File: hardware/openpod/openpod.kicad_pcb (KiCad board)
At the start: 2 copper layers, 42.8 x 59.9 mm, 14 parts, among them J1 SJ-43515TS-SMT-TR

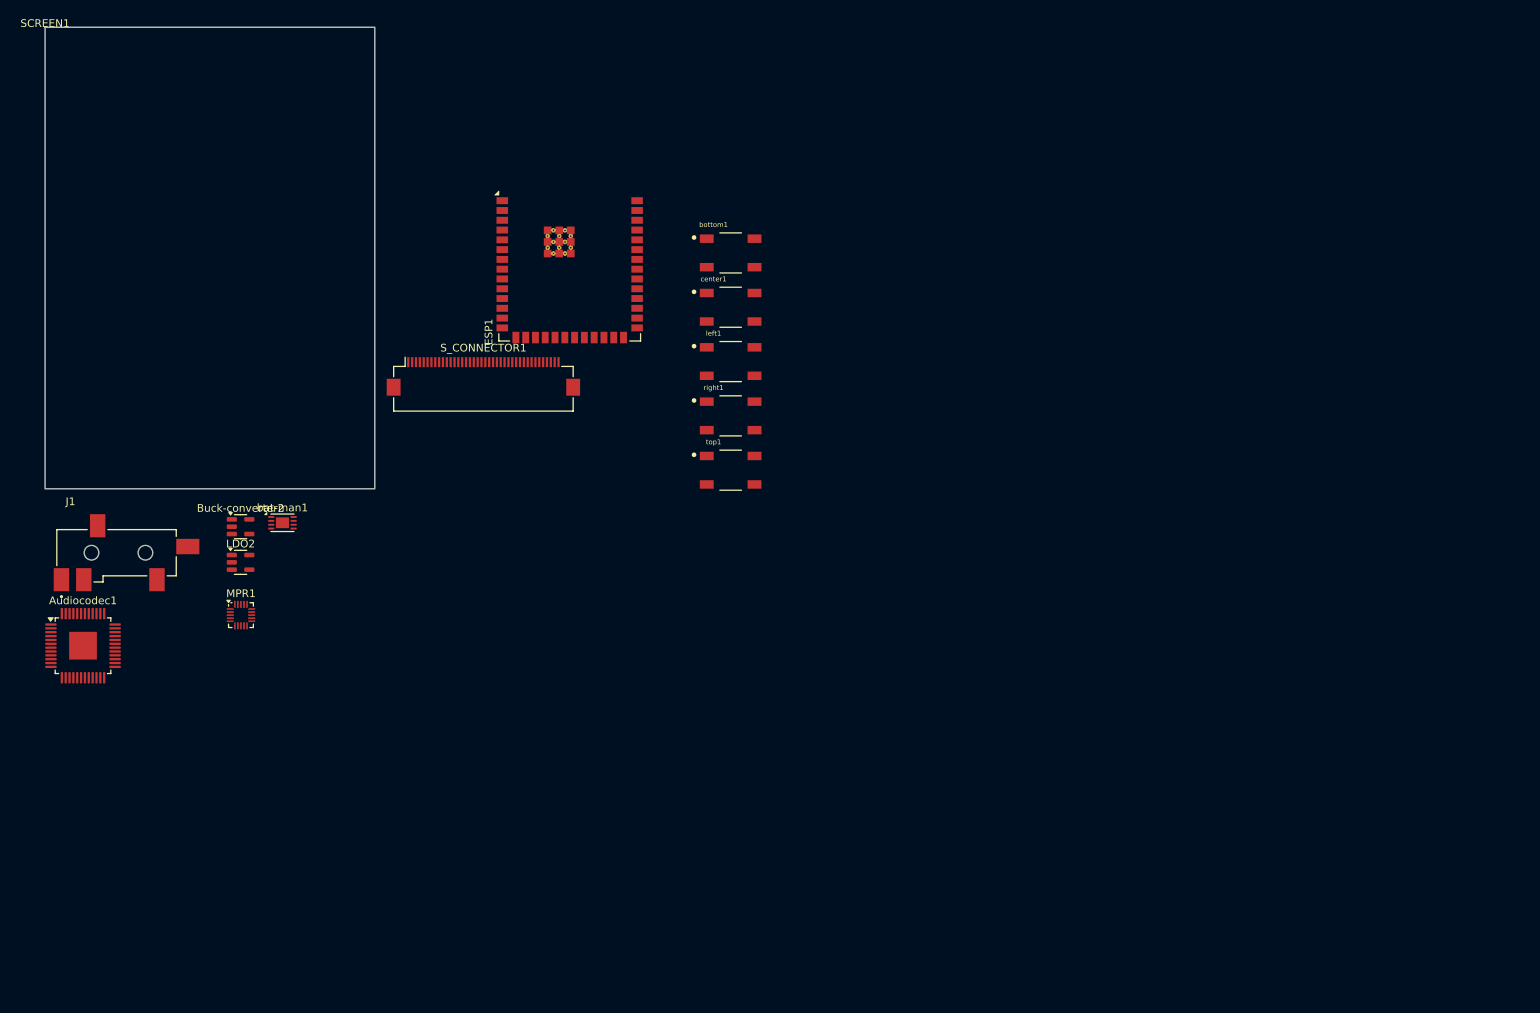
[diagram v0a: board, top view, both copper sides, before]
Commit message: designed clickwheel and see if mpr121 can fit on it
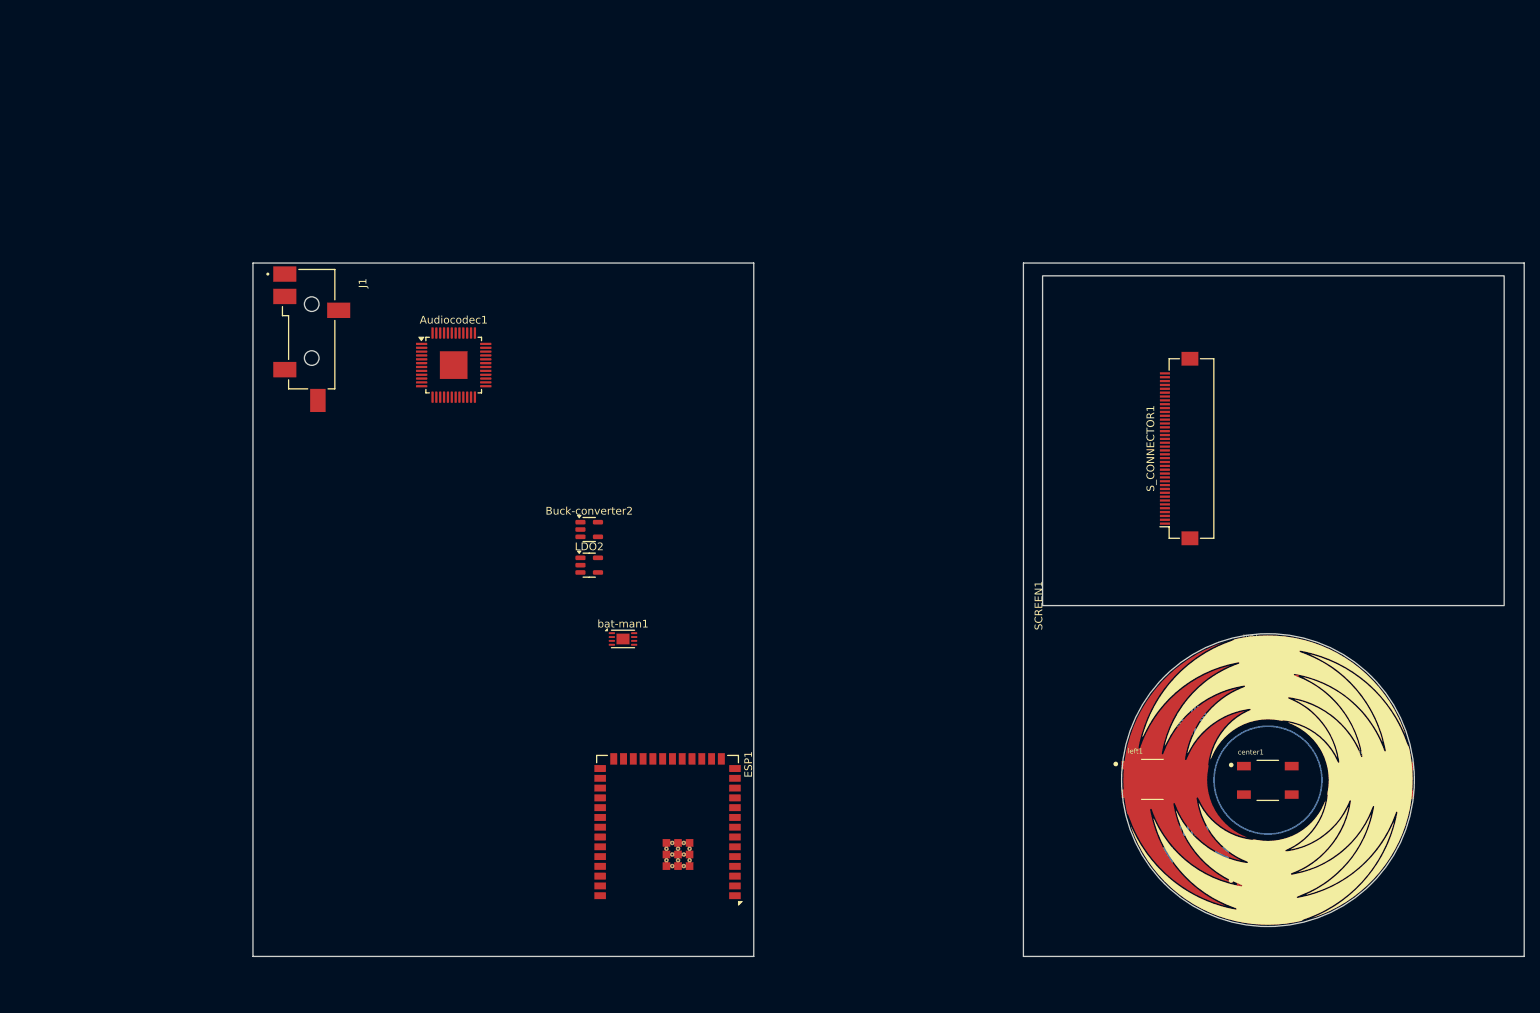
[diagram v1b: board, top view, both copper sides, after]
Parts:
- added Clickwheel1: ~, openpod:clickwheel_1, F.Cu at (231.7, 117.1)
- added clickwheel-connector1: ~, Connector_FFC-FPC:Hirose_FH12-8S-0.5SH_1x08-1MP_P0.50mm_Horizontal, B.Cu at (222.1, 125.5)
- ESP1: footprint openpod:ESP32-S3-WROOM-2 -> RF_Module:ESP32-S3-WROOM-2
- MPR1: footprint Package_DFN_QFN:UQFN-20_3x3mm_P0.4mm -> openpod:mpr121qr2; moved to B.Cu
- moved SCREEN1 149.7 mm to (202.5, 94.5), turned to 90 degrees
- moved MPR1 124.2 mm to (221.9, 109.3), turned to 90 degrees
- moved bottom1 108.7 mm to (231.7, 132.1)
- moved right1 97.0 mm to (246.7, 117.1)
- moved center1 92.9 mm to (231.7, 117.1)
- moved S_CONNECTOR1 90.8 mm to (220.2, 74.1), turned to 90 degrees
- moved ESP1 80.7 mm to (153.8, 126.9), turned to 180 degrees
- moved left1 77.1 mm to (216.7, 117.0)
- moved top1 74.2 mm to (231.7, 102.2)
- moved Audiocodec1 60.3 mm to (126.1, 63.2)
- moved J1 49.1 mm to (104.1, 51.4), turned to -90 degrees
- moved bat-man1 46.7 mm to (148.0, 98.8)
- moved Buck-converter2 45.3 mm to (143.6, 84.6)
- moved LDO2 45.3 mm to (143.6, 89.2)
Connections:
- MPR1 pad 1: unconnected-(MPR1-~{IRQ}-Pad1) -> Net-(MPR1-~{IRQ})
- MPR1 pad 15: unconnected-(MPR1-LED3/ELE7-Pad15) -> Net-(Clickwheel1-right)
- MPR1 pad 16: unconnected-(MPR1-LED4/ELE8-Pad16) -> Net-(Clickwheel1-top)
- MPR1 pad 19: unconnected-(MPR1-LED7/ELE11-Pad19) -> Net-(Clickwheel1-bottom)
- MPR1 pad 2: unconnected-(MPR1-SCL-Pad2) -> Net-(MPR1-SCL)
- MPR1 pad 20: unconnected-(MPR1-VDD-Pad20) -> Net-(MPR1-VDD)
- MPR1 pad 3: unconnected-(MPR1-SDA-Pad3) -> Net-(MPR1-SDA)
- MPR1 pad 4: unconnected-(MPR1-ADDR-Pad4) -> Net-(MPR1-ADDR)
- MPR1 pad 5: unconnected-(MPR1-VREG-Pad5) -> Net-(MPR1-VREG)
- MPR1 pad 6: unconnected-(MPR1-VSS-Pad6) -> Net-(MPR1-VSS)
- MPR1 pad 7: unconnected-(MPR1-REXT-Pad7) -> Net-(MPR1-REXT)
- MPR1 pad 9: unconnected-(MPR1-ELE1-Pad9) -> Net-(Clickwheel1-left)
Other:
- board size 42.8 x 59.9 mm -> 165 x 90 mm

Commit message: update power and audio
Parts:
- moved S_CONNECTOR1 63.4 mm to (157.3, 66.4)
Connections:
- clickwheel-connector1 pad 1: Net-(MPR1-REXT) -> Net-(MPR1-VDD)
- clickwheel-connector1 pad 2: Net-(MPR1-VSS) -> Net-(MPR1-~{IRQ})
- clickwheel-connector1 pad 3: Net-(MPR1-VREG) -> Net-(MPR1-SCL)
- clickwheel-connector1 pad 4: Net-(MPR1-ADDR) -> Net-(MPR1-SDA)
- clickwheel-connector1 pad 5: Net-(MPR1-SDA) -> Net-(MPR1-ADDR)
- clickwheel-connector1 pad 6: Net-(MPR1-SCL) -> Net-(MPR1-VREG)
- clickwheel-connector1 pad 7: Net-(MPR1-~{IRQ}) -> Net-(MPR1-VSS)
- clickwheel-connector1 pad 8: Net-(MPR1-VDD) -> Net-(MPR1-REXT)
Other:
- board size 165 x 90 mm -> 65 x 90 mm
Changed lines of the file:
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@@
     (property "Supplier Part number" "CP-43515TSSJTR-ND")
     (attr smd)
-    (fp_text reference "J1" (at 1.175 -10.135 90) (layer "F.SilkS")
+    (fp_text reference "J1" (at 1.175 -10.135 -90) (layer "F.SilkS")
         (effects (font (size 1 1) (thickness 0.15)))
     )
-    (fp_text value "SJ-43515TS-SMT-TR" (at 11.335 3.135 90) (layer "F.Fab")
+    (fp_text value "SJ-43515TS-SMT-TR" (at 11.335 3.135 -90) (layer "F.Fab")
         (effects (font (size 1 1) (thickness 0.15)))
     )
@@
   )
   (footprint "openpod:Hirose_FH12-40S-0.5SH_1x40-1MP_P0.50mm_Horizontal" (layer "F.Cu")
-    (at 220.215 74.075 90)
+    (at 157.298 66.378 90)
     (descr "Hirose FH12, FFC/FPC connector, FH12-40S-0.5SH, 40 Pins per row (https://www.hirose.com/product/en/products/FH12/FH12-24S-0.5SH(55)/), generated with kicad-footprint-generator")
     (tags "connector Hirose FH12 horizontal")
@@
     (descr "Hirose FH12, FFC/FPC connector, FH12-8S-0.5SH, 8 Pins per row (https://www.hirose.com/product/en/products/FH12/FH12-24S-0.5SH(55)/), generated with kicad-footprint-generator")
     (tags "connector Hirose FH12 horizontal")
-    (property "Manufacturer" "")
-    (property "Part number" "")
+    (property "Manufacturer" "Hirose")
+    (property "Part number" "FH12-8S-0.5SH(55)")
     (property "Sheetfile" "buttons.kicad_sch")
     (property "Sheetname" "Buttons")
-    (property "Supplier" "")
-    (property "Supplier Part number" "")
+    (property "Supplier" "DigiKey")
+    (property "Supplier Part number" "H124618TR-ND")
     (attr smd)
     (fp_text reference "clickwheel-connector1" (at 0 3.7) (layer "B.SilkS")
@@
       (stroke (width 0.1) (type solid)) (layer "B.Fab"))
     (pad "1" smd rect (at -1.75 1.85 180) (size 0.3 1.3) (layers "B.Cu" "B.Paste" "B.Mask")
+      (net 150 "Net-(MPR1-VDD)") (pinfunction "VDD") (pintype "power_in"))
+    (pad "2" smd rect (at -1.25 1.85 180) (size 0.3 1.3) (layers "B.Cu" "B.Paste" "B.Mask")
+      (net 139 "Net-(MPR1-~{IRQ})") (pinfunction "IRQ") (pintype "input"))
+    (pad "3" smd rect (at -0.75 1.85 180) (size 0.3 1.3) (layers "B.Cu" "B.Paste" "B.Mask")
+      (net 140 "Net-(MPR1-SCL)") (pinfunction "SCL") (pintype "input"))
+    (pad "4" smd rect (at -0.25 1.85 180) (size 0.3 1.3) (layers "B.Cu" "B.Paste" "B.Mask")
+      (net 141 "Net-(MPR1-SDA)") (pinfunction "SDA") (pintype "bidirectional"))
+    (pad "5" smd rect (at 0.25 1.85 180) (size 0.3 1.3) (layers "B.Cu" "B.Paste" "B.Mask")
+      (net 142 "Net-(MPR1-ADDR)") (pinfunction "ADDR") (pintype "input"))
+    (pad "6" smd rect (at 0.75 1.85 180) (size 0.3 1.3) (layers "B.Cu" "B.Paste" "B.Mask")
+      (net 143 "Net-(MPR1-VREG)") (pinfunction "VREG") (pintype "input"))
+    (pad "7" smd rect (at 1.25 1.85 180) (size 0.3 1.3) (layers "B.Cu" "B.Paste" "B.Mask")
+      (net 144 "Net-(MPR1-VSS)") (pinfunction "VSS") (pintype "power_in"))
+    (pad "8" smd rect (at 1.75 1.85 180) (size 0.3 1.3) (layers "B.Cu" "B.Paste" "B.Mask")
       (net 145 "Net-(MPR1-REXT)") (pinfunction "REXT") (pintype "passive"))
-    (pad "2" smd rect (at -1.25 1.85 180) (size 0.3 1.3) (layers "B.Cu" "B.Paste" "B.Mask")
-      (net 144 "Net-(MPR1-VSS)") (pinfunction "VSS") (pintype "power_in"))
-    (pad "3" smd rect (at -0.75 1.85 180) (size 0.3 1.3) (layers "B.Cu" "B.Paste" "B.Mask")
-      (net 143 "Net-(MPR1-VREG)") (pinfunction "VREG") (pintype "input"))
-    (pad "4" smd rect (at -0.25 1.85 180) (size 0.3 1.3) (layers "B.Cu" "B.Paste" "B.Mask")
-      (net 142 "Net-(MPR1-ADDR)") (pinfunction "ADDR") (pintype "input"))
-    (pad "5" smd rect (at 0.25 1.85 180) (size 0.3 1.3) (layers "B.Cu" "B.Paste" "B.Mask")
-      (net 141 "Net-(MPR1-SDA)") (pinfunction "SDA") (pintype "bidirectional"))
-    (pad "6" smd rect (at 0.75 1.85 180) (size 0.3 1.3) (layers "B.Cu" "B.Paste" "B.Mask")
-      (net 140 "Net-(MPR1-SCL)") (pinfunction "SCL") (pintype "input"))
-    (pad "7" smd rect (at 1.25 1.85 180) (size 0.3 1.3) (layers "B.Cu" "B.Paste" "B.Mask")
-      (net 139 "Net-(MPR1-~{IRQ})") (pinfunction "IRQ") (pintype "input"))
-    (pad "8" smd rect (at 1.75 1.85 180) (size 0.3 1.3) (layers "B.Cu" "B.Paste" "B.Mask")
-      (net 150 "Net-(MPR1-VDD)") (pinfunction "VDD") (pintype "power_in"))
     (pad "MP" smd rect (at -3.65 -1.4 180) (size 1.8 2.2) (layers "B.Cu" "B.Paste" "B.Mask"))
     (pad "MP" smd rect (at 3.65 -1.4 180) (size 1.8 2.2) (layers "B.Cu" "B.Paste" "B.Mask"))
@@
   (gr_rect (start 200 50) (end 265 140)
     (stroke (width 0.1) (type default)) (fill none) (layer "Edge.Cuts"))
+  (gr_rect (start 102.438 51.689) (end 162.382 94.488)
+    (stroke (width 0.1) (type default)) (fill none) (layer "User.1"))
+  (gr_circle (center 131.7 117) (end 150.7 117)
+    (stroke (width 0.1) (type default)) (fill none) (layer "User.1"))
   (gr_rect (start 100 50) (end 165 140)
-    (stroke (width 0.1) (type default)) (fill none) (layer "Edge.Cuts"))
+    (stroke (width 0.1) (type default)) (fill none) (layer "User.1"))
+  (group "" (id 2323effc-a0d1-4313-aa63-f355f6ec8b0d)
+    (members
+      2688467a-e8e8-472a-93a4-b563cc7689f2
+      444ad04b-41b9-4e0e-83e2-88ab4b3fa3dd
+      a93e316e-5e73-4e58-bea3-ef2f803a2fef
+    )
+  )
 )

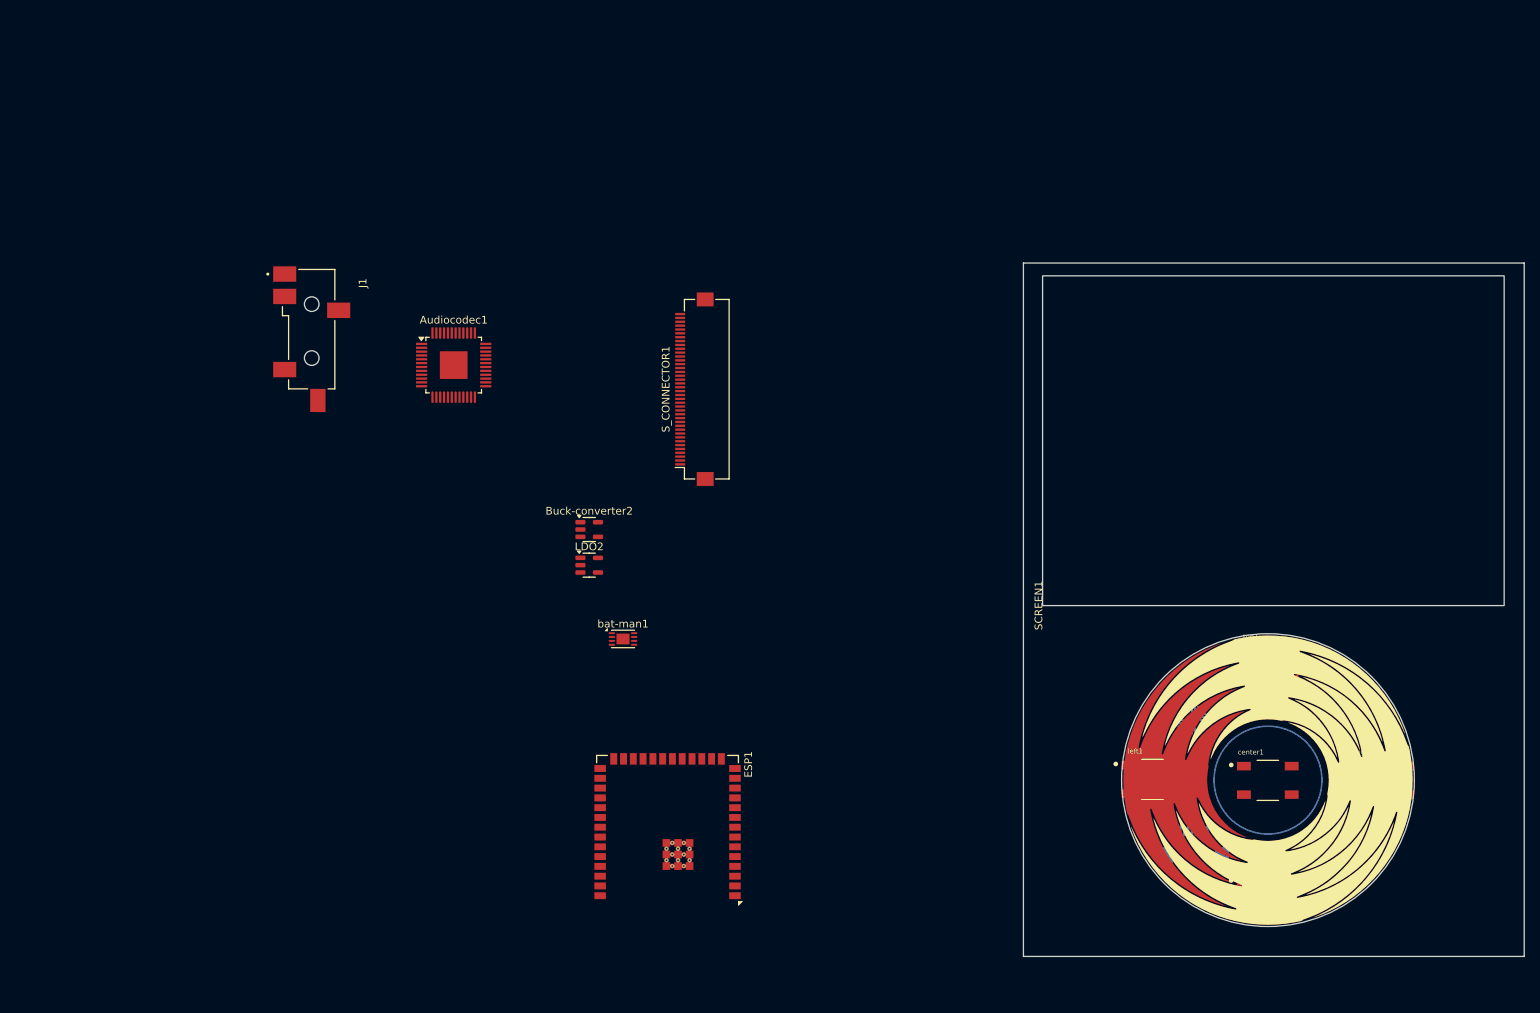
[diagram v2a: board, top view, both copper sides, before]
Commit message: added UART converter
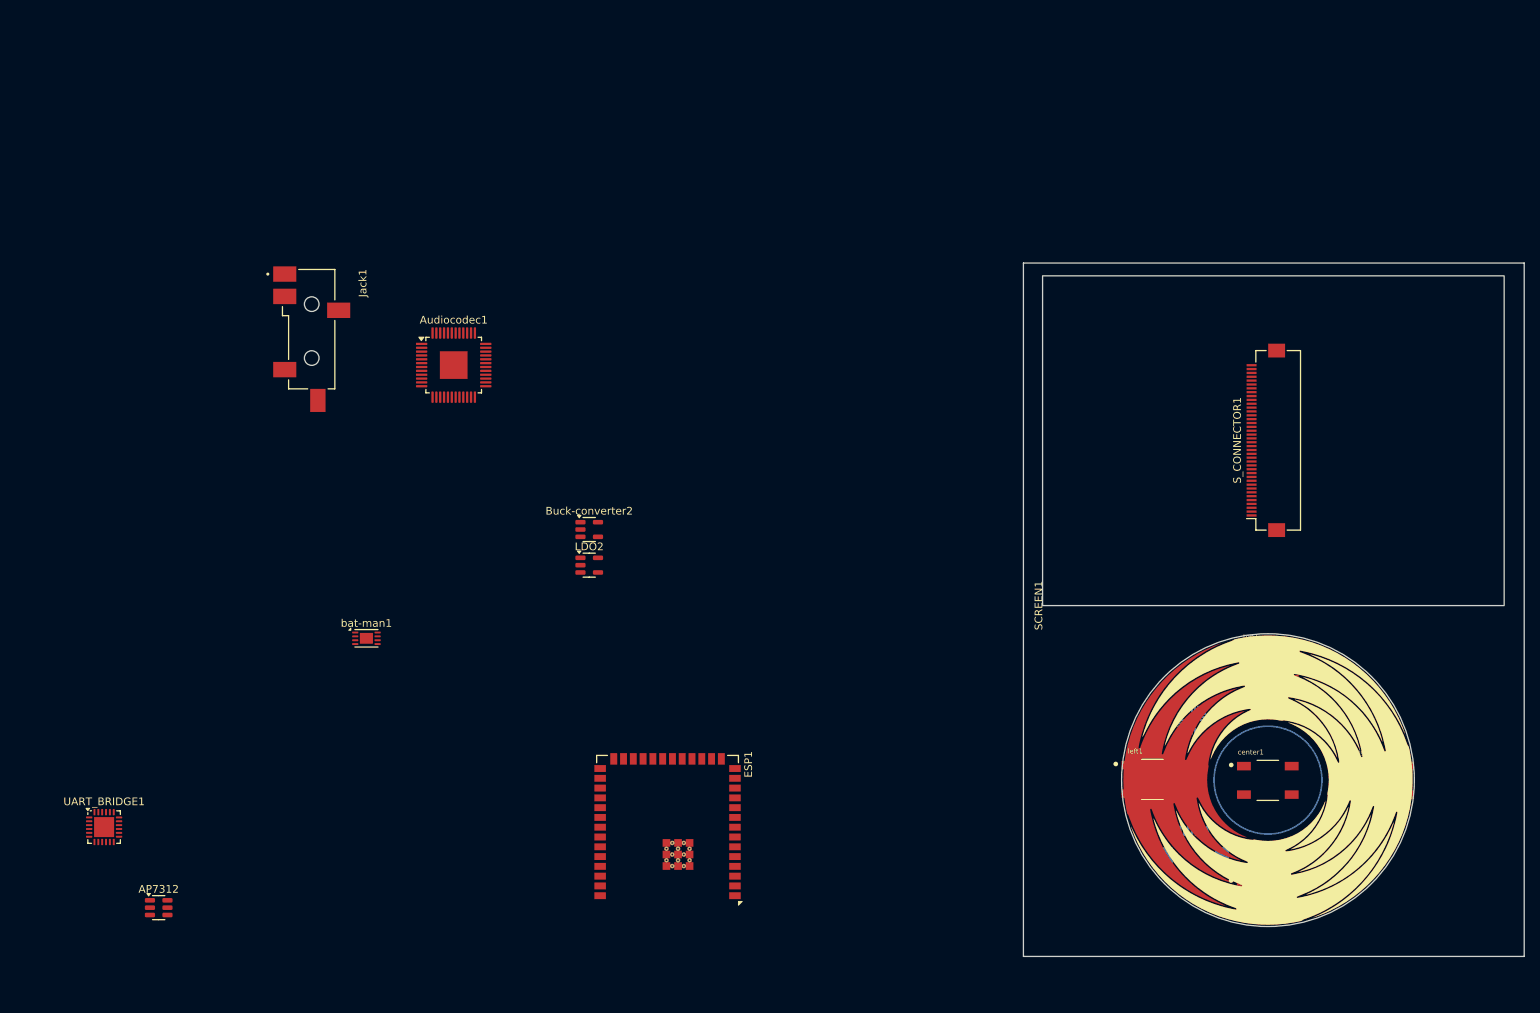
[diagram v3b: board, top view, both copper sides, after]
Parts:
- added AP7312: ~, Package_TO_SOT_SMD:SOT-23-6, F.Cu at (87.8, 133.7)
- added UART_BRIDGE1: CP2102N-Axx-xQFN24, Package_DFN_QFN:QFN-24-1EP_4x4mm_P0.5mm_EP2.6x2.6mm, F.Cu at (80.7, 123.2)
- moved S_CONNECTOR1 74.5 mm to (231.5, 73.0)
- moved bat-man1 33.3 mm to (114.7, 98.7)
- renumbered J1 to Jack1
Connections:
- net Net-(BT2-+) renamed VBAT
- Buck-converter2 pad 3: 3.3V -> Net-(Buck-converter2-EN)
- Buck-converter2 pad 4: 3.3V -> Net-(Buck-converter2-EN)
- Jack1 pad 1: Net-(Audiocodec1-GBUF) -> Net-(VS1-GBUF)
- Jack1 pad 2: Net-(Audiocodec1-LEFT) -> Net-(VS1-LEFT)
- Jack1 pad 3: Net-(Audiocodec1-RIGHT) -> Net-(VS1-RIGHT)
- Jack1 pad 4: Net-(Audiocodec1-RIGHT) -> Net-(VS1-RIGHT)
